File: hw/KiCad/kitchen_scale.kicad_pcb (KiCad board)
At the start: 2 copper layers, 60 x 50 mm, 12 parts, among them J1 Conn_01x08_Socket, J2 Conn_HX711, J3 Conn_01x04_Pin, SW1 SW_Push, SW2 SW_SPST, SW3 SW_Push, SW4 SW_Push, U1 DEBO1_3_7LI_1_0A charge_contr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, U2 WeMos_D1_mini, U3 LF33_TO220

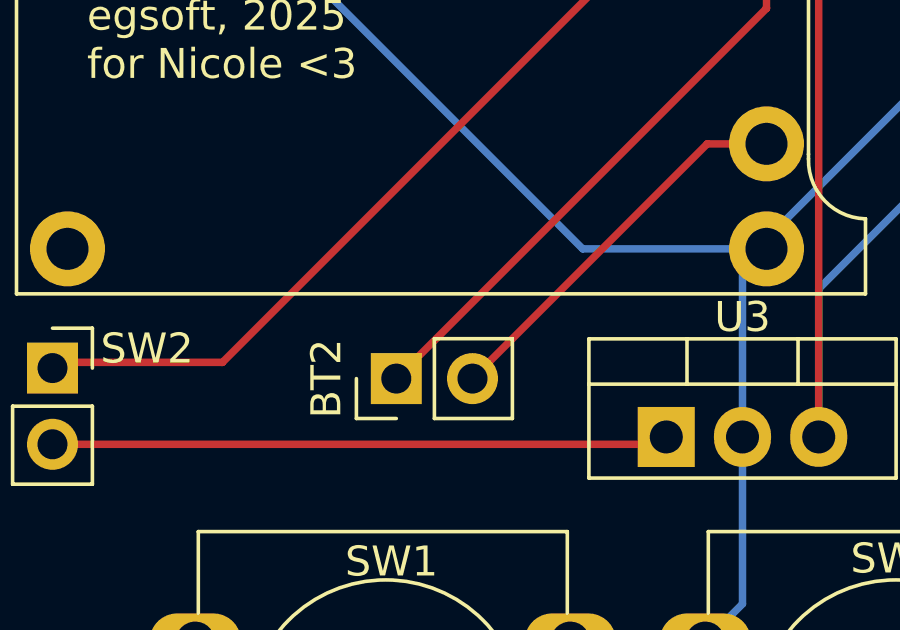
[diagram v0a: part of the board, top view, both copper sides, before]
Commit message: Add battery signs
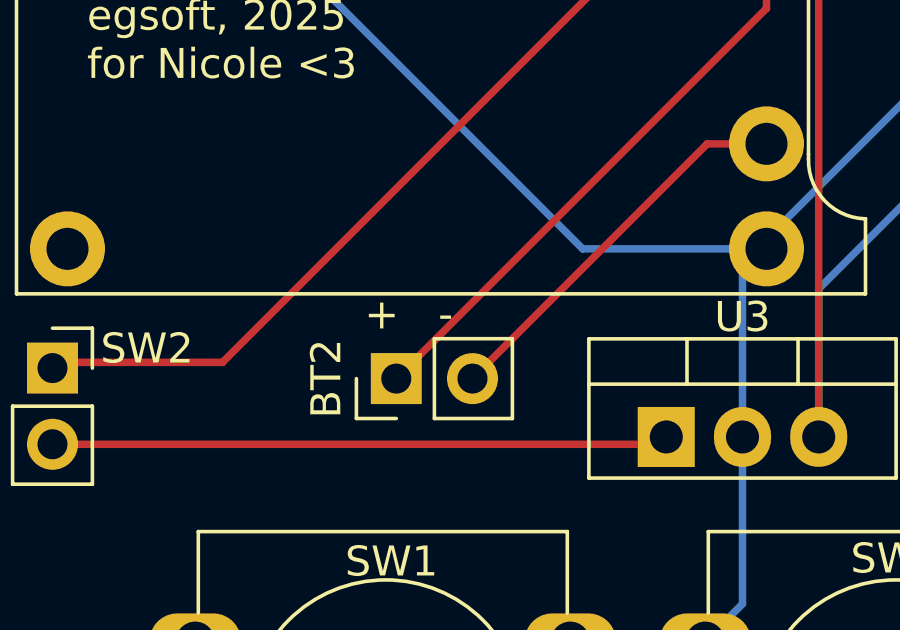
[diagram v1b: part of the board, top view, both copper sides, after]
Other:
- board text added: "+ -"
- board text added: "- +"
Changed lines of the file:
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@@
   (gr_rect (start 60 75) (end 120 125)
     (stroke (width 0.1) (type default)) (fill none) (layer "Edge.Cuts"))
+  (gr_text "-   +" (at 77.2 105.2) (layer "B.SilkS")
+    (effects (font (size 1 1) (thickness 0.15)) (justify left bottom mirror))
+  )
+  (gr_text "+   -" (at 72.4 105.2) (layer "F.SilkS")
+    (effects (font (size 1 1) (thickness 0.15)) (justify left bottom))
+  )
   (gr_text "Kitchen Scale 2.0\negsoft, 2025\nfor Nicole <3" (at 63.15 96.85) (layer "F.SilkS")
     (effects (font (size 1 1) (thickness 0.15)) (justify left bottom))
